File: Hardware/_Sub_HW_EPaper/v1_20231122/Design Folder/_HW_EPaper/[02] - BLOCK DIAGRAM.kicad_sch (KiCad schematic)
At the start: 0 parts

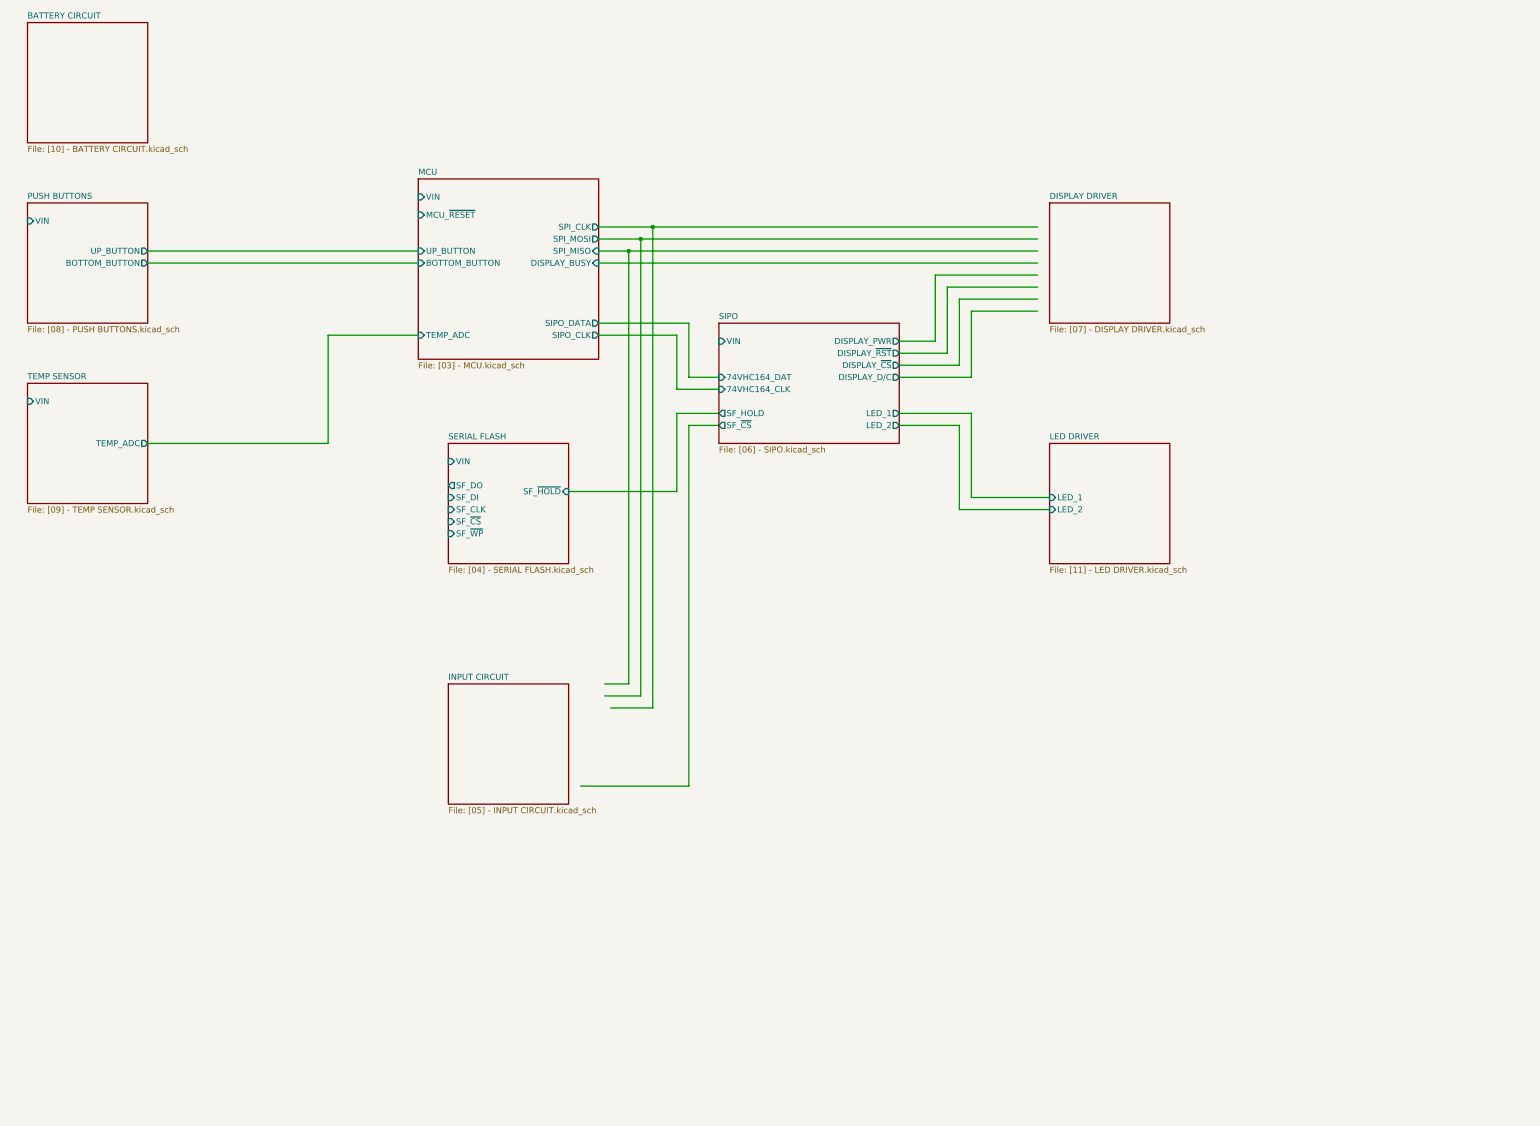
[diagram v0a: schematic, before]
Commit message: Working on E-Paper schematic
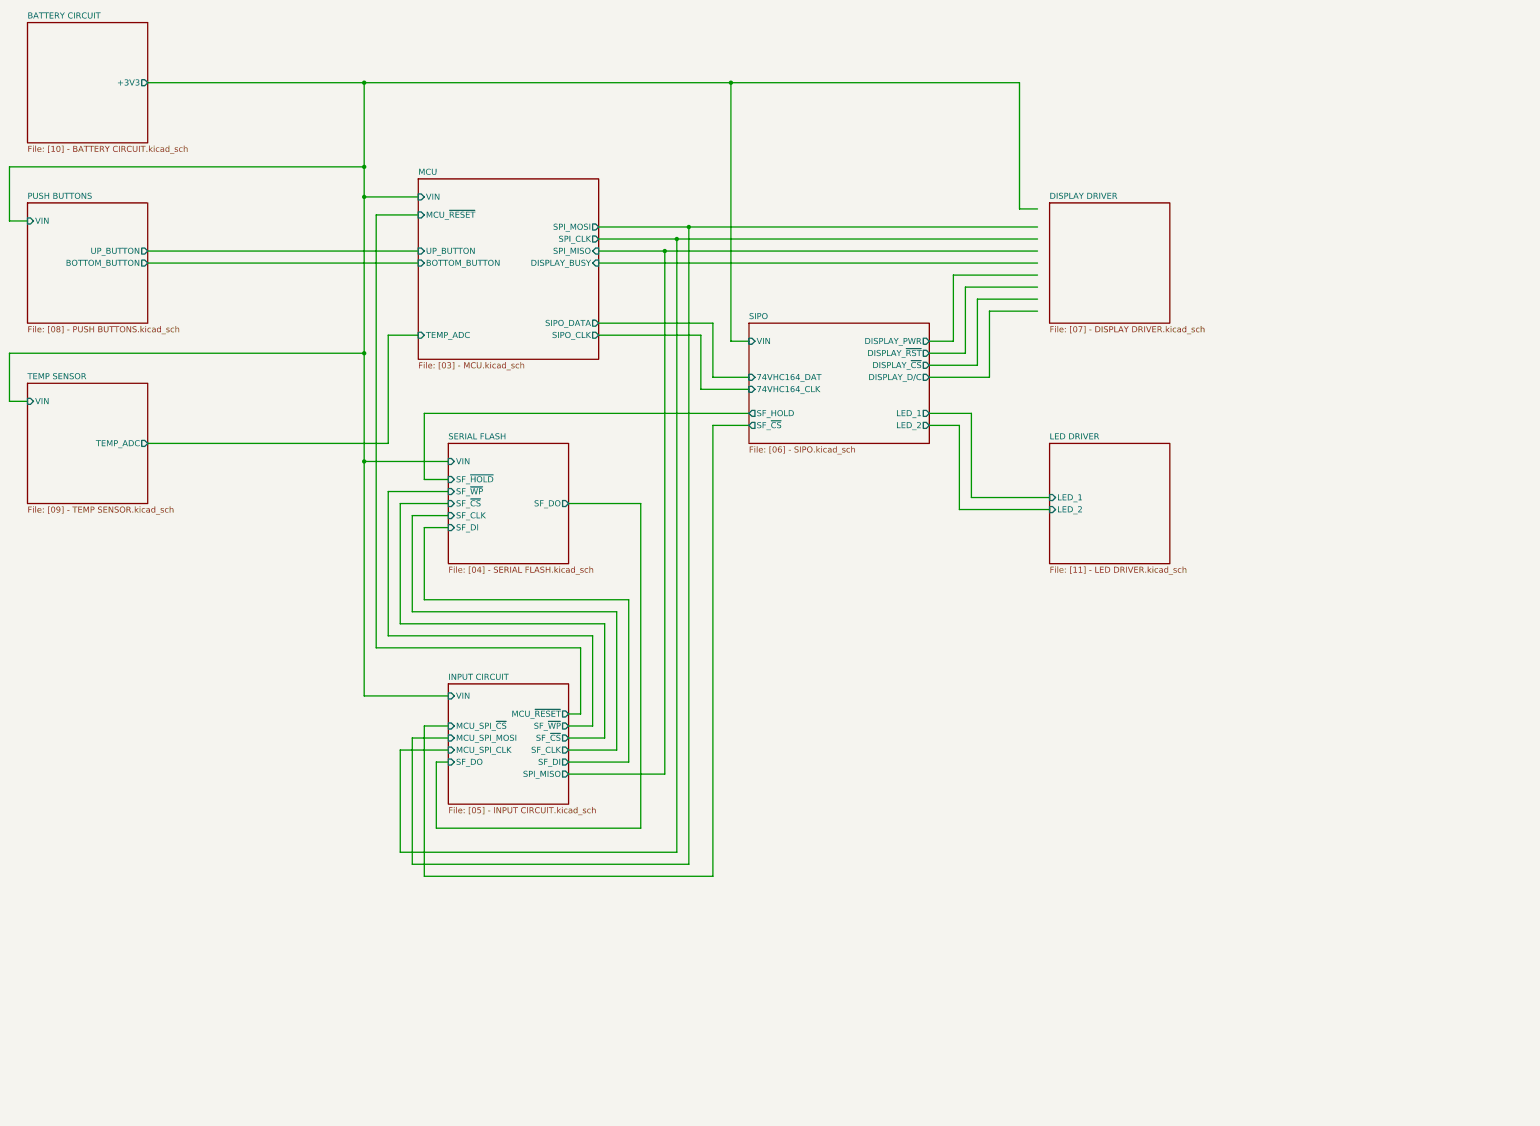
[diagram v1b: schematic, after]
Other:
- sheet BATTERY CIRCUIT ports: added +3V3; removed none
- sheet INPUT CIRCUIT ports: added MCU_SPI_CLK, MCU_SPI_MOSI, MCU_SPI_~{CS}, MCU_~{RESET}, SF_CLK, SF_DI, SF_DO, SF_~{CS}, SF_~{WP}, SPI_MISO, VIN; removed none

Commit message: EPaper schematic is almost done...
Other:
- sheet BATTERY CIRCUIT ports: added V_BATT; removed +3V3
- sheet DISPLAY DRIVER ports: added E24_BUSY, E24_DC, E24_RST, E24_~{CS}, PWR, SPI_CLK, SPI_SDO, VIN; removed none
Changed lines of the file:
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@@
   (junction (at 172.72 156.21) (diameter 0) (color 0 0 0 0)
   )
-  (junction (at 236.22 111.76) (diameter 0) (color 0 0 0 0)
-  )
   (junction (at 172.72 93.98) (diameter 0) (color 0 0 0 0)
   )
-  (junction (at 238.76 109.22) (diameter 0) (color 0 0 0 0)
-  )
-  (junction (at 241.3 106.68) (diameter 0) (color 0 0 0 0)
+  (junction (at 238.76 113.03) (diameter 0) (color 0 0 0 0)
+  )
+  (junction (at 241.3 110.49) (diameter 0) (color 0 0 0 0)
+  )
+  (wire (pts (xy 238.76 113.03) (xy 238.76 238.76))
+    (stroke (width 0) (type default))
   )
   (wire (pts (xy 180.34 165.1) (xy 190.5 165.1))
@@
     (stroke (width 0) (type default))
   )
+  (wire (pts (xy 304.8 124.46) (xy 317.5 124.46))
+    (stroke (width 0) (type default))
+  )
   (wire (pts (xy 231.14 233.68) (xy 187.96 233.68))
     (stroke (width 0) (type default))
@@
     (stroke (width 0) (type default))
   )
-  (wire (pts (xy 241.3 106.68) (xy 241.3 241.3))
-    (stroke (width 0) (type default))
-  )
   (wire (pts (xy 254 130.81) (xy 250.19 130.81))
     (stroke (width 0) (type default))
@@
     (stroke (width 0) (type default))
   )
-  (wire (pts (xy 297.18 116.84) (xy 314.96 116.84))
+  (wire (pts (xy 297.18 116.84) (xy 317.5 116.84))
     (stroke (width 0) (type default))
   )
@@
     (stroke (width 0) (type default))
   )
-  (wire (pts (xy 304.8 124.46) (xy 314.96 124.46))
-    (stroke (width 0) (type default))
-  )
   (wire (pts (xy 226.06 187.96) (xy 182.88 187.96))
     (stroke (width 0) (type default))
@@
     (stroke (width 0) (type default))
   )
-  (wire (pts (xy 311.15 76.2) (xy 311.15 102.87))
+  (wire (pts (xy 311.15 76.2) (xy 311.15 104.14))
     (stroke (width 0) (type default))
   )
@@
     (stroke (width 0) (type default))
   )
-  (wire (pts (xy 241.3 106.68) (xy 314.96 106.68))
-    (stroke (width 0) (type default))
-  )
-  (wire (pts (xy 299.72 119.38) (xy 314.96 119.38))
+  (wire (pts (xy 241.3 110.49) (xy 317.5 110.49))
+    (stroke (width 0) (type default))
+  )
+  (wire (pts (xy 299.72 119.38) (xy 317.5 119.38))
     (stroke (width 0) (type default))
   )
@@
     (stroke (width 0) (type default))
   )
-  (wire (pts (xy 236.22 111.76) (xy 314.96 111.76))
-    (stroke (width 0) (type default))
-  )
   (wire (pts (xy 220.98 212.09) (xy 220.98 193.04))
     (stroke (width 0) (type default))
@@
     (stroke (width 0) (type default))
   )
-  (wire (pts (xy 236.22 111.76) (xy 236.22 222.25))
+  (wire (pts (xy 236.22 115.57) (xy 236.22 222.25))
     (stroke (width 0) (type default))
   )
@@
     (stroke (width 0) (type default))
   )
-  (wire (pts (xy 302.26 121.92) (xy 314.96 121.92))
+  (wire (pts (xy 302.26 121.92) (xy 317.5 121.92))
     (stroke (width 0) (type default))
   )
@@
     (stroke (width 0) (type default))
   )
-  (wire (pts (xy 238.76 109.22) (xy 238.76 238.76))
-    (stroke (width 0) (type default))
-  )
   (wire (pts (xy 246.38 243.84) (xy 246.38 148.59))
     (stroke (width 0) (type default))
@@
     (stroke (width 0) (type default))
   )
-  (wire (pts (xy 238.76 109.22) (xy 314.96 109.22))
-    (stroke (width 0) (type default))
-  )
-  (wire (pts (xy 238.76 109.22) (xy 222.25 109.22))
+  (wire (pts (xy 238.76 113.03) (xy 317.5 113.03))
+    (stroke (width 0) (type default))
+  )
+  (wire (pts (xy 238.76 113.03) (xy 222.25 113.03))
     (stroke (width 0) (type default))
   )
@@
     (stroke (width 0) (type default))
   )
-  (wire (pts (xy 222.25 114.3) (xy 314.96 114.3))
+  (wire (pts (xy 222.25 107.95) (xy 317.5 107.95))
     (stroke (width 0) (type default))
   )
@@
     (stroke (width 0) (type default))
   )
+  (wire (pts (xy 241.3 110.49) (xy 241.3 241.3))
+    (stroke (width 0) (type default))
+  )
   (wire (pts (xy 226.06 217.17) (xy 226.06 187.96))
     (stroke (width 0) (type default))
@@
     (stroke (width 0) (type default))
   )
-  (wire (pts (xy 222.25 111.76) (xy 236.22 111.76))
-    (stroke (width 0) (type default))
-  )
-  (wire (pts (xy 311.15 102.87) (xy 314.96 102.87))
+  (wire (pts (xy 222.25 115.57) (xy 236.22 115.57))
+    (stroke (width 0) (type default))
+  )
+  (wire (pts (xy 311.15 104.14) (xy 317.5 104.14))
     (stroke (width 0) (type default))
   )
@@
     (stroke (width 0) (type default))
   )
-  (wire (pts (xy 241.3 106.68) (xy 222.25 106.68))
+  (wire (pts (xy 241.3 110.49) (xy 222.25 110.49))
     (stroke (width 0) (type default))
   )
@@
       (effects (font (size 1.27 1.27)) (justify left))
     )
-    (pin "SPI_CLK" output (at 222.25 109.22 0)
-      (effects (font (size 1.27 1.27)) (justify right))
-    )
-    (pin "DISPLAY_BUSY" input (at 222.25 114.3 0)
-      (effects (font (size 1.27 1.27)) (justify right))
-    )
-    (pin "SPI_MOSI" output (at 222.25 106.68 0)
-      (effects (font (size 1.27 1.27)) (justify right))
-    )
-    (pin "SPI_MISO" input (at 222.25 111.76 0)
+    (pin "SPI_CLK" output (at 222.25 113.03 0)
+      (effects (font (size 1.27 1.27)) (justify right))
+    )
+    (pin "DISPLAY_BUSY" input (at 222.25 107.95 0)
+      (effects (font (size 1.27 1.27)) (justify right))
+    )
+    (pin "SPI_MOSI" output (at 222.25 110.49 0)
+      (effects (font (size 1.27 1.27)) (justify right))
+    )
+    (pin "SPI_MISO" input (at 222.25 115.57 0)
       (effects (font (size 1.27 1.27)) (justify right))
     )
@@
       (effects (font (size 1.27 1.27)) (justify left top))
     )
+    (pin "SPI_SDO" input (at 317.5 110.49 180)
+      (effects (font (size 1.27 1.27)) (justify left))
+    )
+    (pin "E24_~{CS}" input (at 317.5 121.92 180)
+      (effects (font (size 1.27 1.27)) (justify left))
+    )
+    (pin "E24_RST" input (at 317.5 119.38 180)
+      (effects (font (size 1.27 1.27)) (justify left))
+    )
+    (pin "E24_DC" input (at 317.5 124.46 180)
+      (effects (font (size 1.27 1.27)) (justify left))
+    )
+    (pin "SPI_CLK" input (at 317.5 113.03 180)
+      (effects (font (size 1.27 1.27)) (justify left))
+    )
+    (pin "E24_BUSY" bidirectional (at 317.5 107.95 180)
+      (effects (font (size 1.27 1.27)) (justify left))
+    )
+    (pin "VIN" input (at 317.5 104.14 180)
+      (effects (font (size 1.27 1.27)) (justify left))
+    )
+    (pin "PWR" input (at 317.5 116.84 180)
+      (effects (font (size 1.27 1.27)) (justify left))
+    )
     (instances
       (project "_HW_EPaper"
@@
       (effects (font (size 1.27 1.27)) (justify left top))
     )
-    (pin "+3V3" output (at 127 76.2 0)
-      (effects (font (size 1.27 1.27)) (justify right))
-    )
+    (pin "V_BATT" output (at 127 76.2 0)
+      (effects (font (size 1.27 1.27)) (justify right))
+    )

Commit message: Updating Hardware File structures
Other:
- sheet BATTERY CIRCUIT renamed BATTERY CHARGER
- sheet MCU renamed MICROCONTROLLER
- sheet SIPO renamed SHIFT REGISTER (SIPO)
- sheet BATTERY CHARGER: file [10] - BATTERY CIRCUIT.kicad_sch -> [10] - BATTERY CHARGER.kicad_sch
- sheet MICROCONTROLLER: file [03] - MCU.kicad_sch -> [03] - MICROCONTROLLER.kicad_sch
- sheet SHIFT REGISTER (SIPO): file [06] - SIPO.kicad_sch -> [06] -SHIFT REGISTER (SIPO).kicad_sch
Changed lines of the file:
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@@
   (title_block
     (title "_HW_EPaper")
+    (date "2023-12-18")
     (rev "v1.0")
     (company "Mend0z0")
     (comment 1 "v1.0")
     (comment 2 "CHECKED")
+    (comment 3 "Siavash Taher Parvar")
+    (comment 4 "_BOM_EPaper.csv")
+    (comment 5 "_HW_EPaper.kicad_pcb")
+    (comment 6 "_GBR_EPaper.zip")
+    (comment 7 "_ASM_EPaper.html")
+    (comment 8 "N/A")
+    (comment 9 "First Release")
   )
   (junction (at 306.07 127) (diameter 0) (color 0 0 0 0)
@@
     (stroke (width 0.1524) (type solid))
     (fill (color 0 0 0 0.0000))
-    (property "Sheetname" "SIPO" (at 309.88 177.0884 0)
-      (effects (font (size 1.27 1.27)) (justify left bottom))
-    )
-    (property "Sheetfile" "[06] - SIPO.kicad_sch" (at 309.88 203.7846 0)
+    (property "Sheetname" "SHIFT REGISTER (SIPO)" (at 309.88 177.0884 0)
+      (effects (font (size 1.27 1.27)) (justify left bottom))
+    )
+    (property "Sheetfile" "[06] -SHIFT REGISTER (SIPO).kicad_sch" (at 309.88 203.7846 0)
       (effects (font (size 1.27 1.27)) (justify left top))
     )
@@
     (stroke (width 0.1524) (type solid))
     (fill (color 0 0 0 0.0000))
-    (property "Sheetname" "MCU" (at 240.03 146.6084 0)
-      (effects (font (size 1.27 1.27)) (justify left bottom))
-    )
-    (property "Sheetfile" "[03] - MCU.kicad_sch" (at 240.03 186.0046 0)
+    (property "Sheetname" "MICROCONTROLLER" (at 240.03 146.6084 0)
+      (effects (font (size 1.27 1.27)) (justify left bottom))
+    )
+    (property "Sheetfile" "[03] - MICROCONTROLLER.kicad_sch" (at 240.03 186.0046 0)
       (effects (font (size 1.27 1.27)) (justify left top))
     )
@@
     (stroke (width 0.1524) (type solid))
     (fill (color 0 0 0 0.0000))
-    (property "Sheetname" "BATTERY CIRCUIT" (at 157.48 113.5884 0)
-      (effects (font (size 1.27 1.27)) (justify left bottom))
-    )
-    (property "Sheetfile" "[10] - BATTERY CIRCUIT.kicad_sch" (at 157.48 140.2846 0)
-      (effects (font (size 1.27 1.27)) (justify left top))
-    )
+    (property "Sheetname" "BATTERY CHARGER" (at 157.48 113.5884 0)
+      (effects (font (size 1.27 1.27)) (justify left bottom))
+    )
+    (property "Sheetfile" "[10] - BATTERY CHARGER.kicad_sch" (at 157.48 140.2846 0)
+      (effects (font (size 1.27 1.27)) (justify left top))
+    )
